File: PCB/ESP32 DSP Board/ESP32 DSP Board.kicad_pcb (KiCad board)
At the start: 2 copper layers, 67 parts, among them J1 USB4216-03-A_REVA, J2 USB4216-03-A_REVA, SW1 PTS810_SJM_250_SMTR_LFS, SW2 PTS810_SJM_250_SMTR_LFS, U11 INTERFACE-CP2102-GMR_QFN28_, U8 ESP32-S3-WROOM-1, U9 TPS73733DCQ

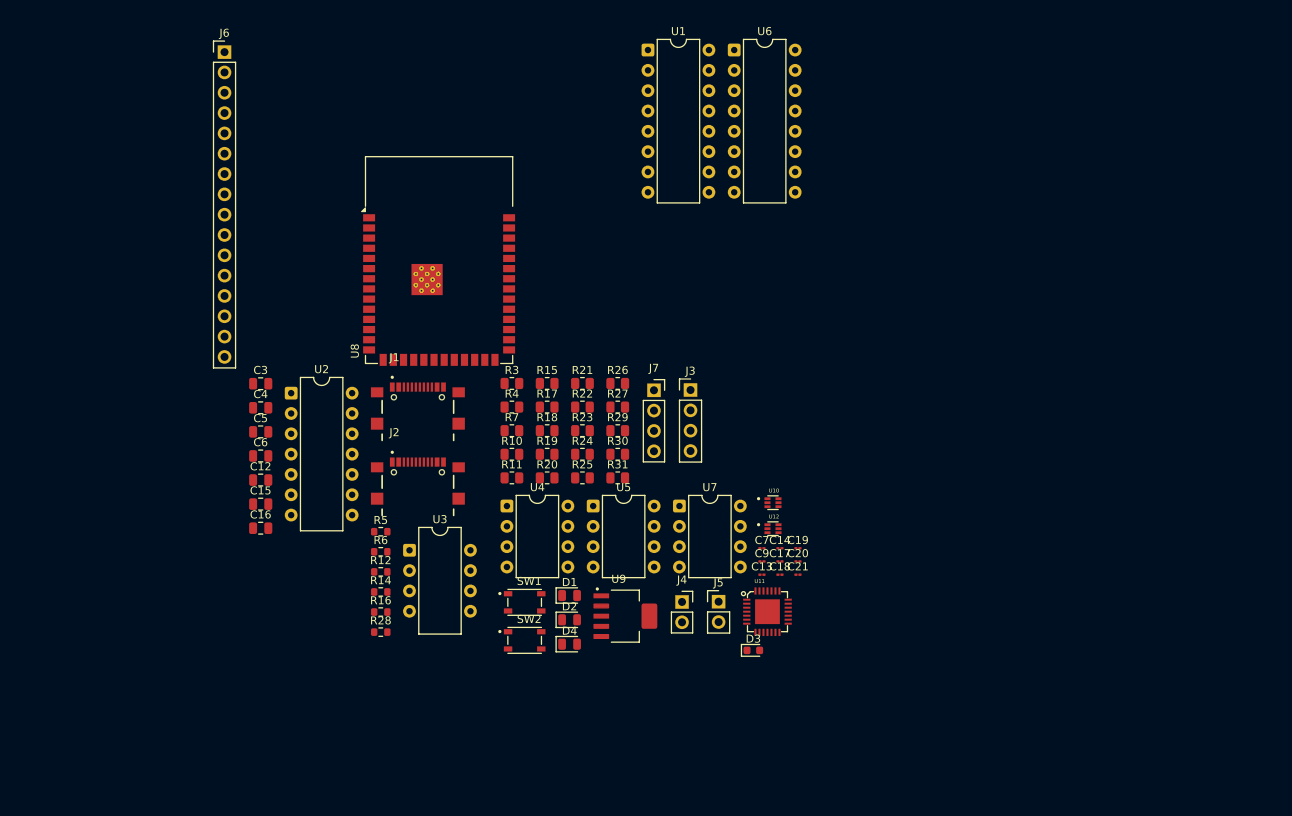
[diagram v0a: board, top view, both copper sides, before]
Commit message: Added clamping and biasing to audio inputs, hpf and rail to rail amplifier to DAC output, 1.5V LDO, footprints updated
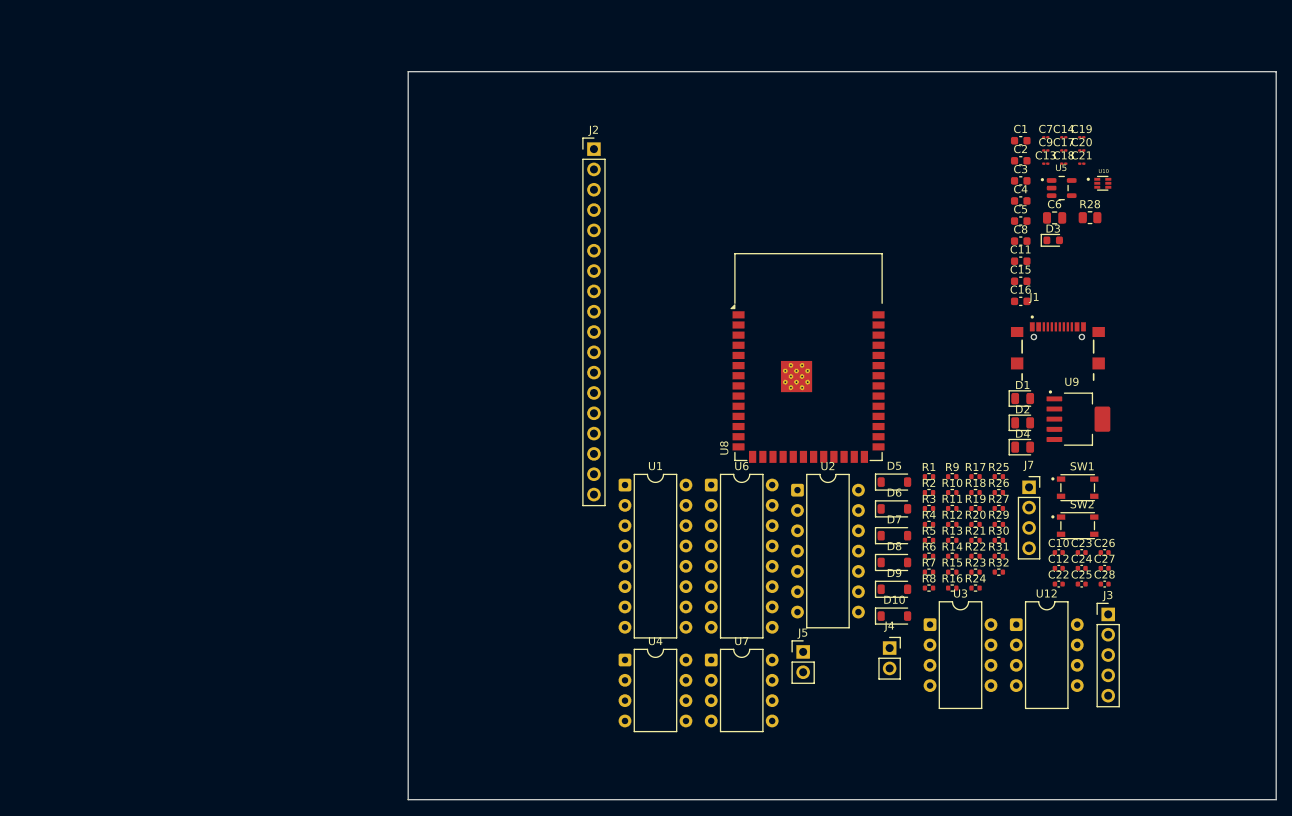
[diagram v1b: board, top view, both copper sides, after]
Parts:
- removed J6: ~, Connector_PinHeader_2.54mm:PinHeader_1x16_P2.54mm_Vertical
- removed U11: INTERFACE-CP2102-GMR_QFN28_, USB-UART-Bridge:CP2102-QFN28G
- added C1: 10uF, Capacitor_SMD:C_0603_1608Metric, F.Cu at (171.1, 55.6)
- added C10: 0.1uF, Capacitor_SMD:C_0402_1005Metric, F.Cu at (175.8, 107.1)
- added C11: 10uF, Capacitor_SMD:C_0603_1608Metric, F.Cu at (171.1, 70.7)
- added C2: 10uF, Capacitor_SMD:C_0603_1608Metric, F.Cu at (171.1, 58.1)
- added C22: 0.1uF, Capacitor_SMD:C_0402_1005Metric, F.Cu at (175.8, 111.0)
- added C23: 0.1uF, Capacitor_SMD:C_0402_1005Metric, F.Cu at (178.7, 107.1)
- added C24: 0.1uF, Capacitor_SMD:C_0402_1005Metric, F.Cu at (178.7, 109.1)
- added C25: 0.1uF, Capacitor_SMD:C_0402_1005Metric, F.Cu at (178.7, 111.0)
- added C26: 0.1uF, Capacitor_SMD:C_0402_1005Metric, F.Cu at (181.6, 107.1)
- added C27: 0.1uF, Capacitor_SMD:C_0402_1005Metric, F.Cu at (181.6, 109.1)
- added C28: 10nF, Capacitor_SMD:C_0402_1005Metric, F.Cu at (181.6, 111.0)
- added C8: 1uF, Capacitor_SMD:C_0603_1608Metric, F.Cu at (171.1, 68.2)
- added D10: D_Zener, Diode_SMD:D_SOD-123, F.Cu at (155.3, 115.0)
- added D5: D_Zener, Diode_SMD:D_SOD-123, F.Cu at (155.3, 98.3)
- added D6: D_Zener, Diode_SMD:D_SOD-123, F.Cu at (155.3, 101.7)
- added D7: D_Zener, Diode_SMD:D_SOD-123, F.Cu at (155.3, 105.0)
- added D8: D_Zener, Diode_SMD:D_SOD-123, F.Cu at (155.3, 108.3)
- added D9: D_Zener, Diode_SMD:D_SOD-123, F.Cu at (155.3, 111.7)
- added R1: 10K, Resistor_SMD:R_0402_1005Metric, F.Cu at (159.6, 97.6)
- added R13: 10K, Resistor_SMD:R_0402_1005Metric, F.Cu at (162.5, 105.6)
- added R2: 10K, Resistor_SMD:R_0402_1005Metric, F.Cu at (159.6, 99.6)
- added R32: 95.3K, Resistor_SMD:R_0402_1005Metric, F.Cu at (168.3, 109.6)
- added R8: 10K, Resistor_SMD:R_0402_1005Metric, F.Cu at (159.6, 111.5)
- added R9: 10K, Resistor_SMD:R_0402_1005Metric, F.Cu at (162.5, 97.6)
- C12: value 10uF -> 0.1uF; footprint Capacitor_SMD:C_0805_2012Metric -> Capacitor_SMD:C_0402_1005Metric
- C15, C16, C3, C4, C5: footprint Capacitor_SMD:C_0805_2012Metric -> Capacitor_SMD:C_0603_1608Metric
- J2: value USB4216-03-A_REVA -> ~; footprint USB_Connector:GCT_USB4216-03-A_REVA -> Connector_PinHeader_2.54mm:PinHeader_1x18_P2.54mm_Vertical
- J3: footprint Connector_PinHeader_2.54mm:PinHeader_1x04_P2.54mm_Vertical -> Connector_PinHeader_2.54mm:PinHeader_1x05_P2.54mm_Vertical
- R10, R11: value 5.1k -> 10K; footprint Resistor_SMD:R_0805_2012Metric -> Resistor_SMD:R_0402_1005Metric
- R12: value 1K -> 10K; footprint Resistor_SMD:R_0603_1608Metric -> Resistor_SMD:R_0402_1005Metric
- R14, R5, R6: footprint Resistor_SMD:R_0603_1608Metric -> Resistor_SMD:R_0402_1005Metric
- R15: value 470 -> 1K; footprint Resistor_SMD:R_0805_2012Metric -> Resistor_SMD:R_0402_1005Metric
- R16: value 220 -> 23.2K; footprint Resistor_SMD:R_0603_1608Metric -> Resistor_SMD:R_0402_1005Metric
- R17, R18, R19, R20, R21, R22, R23, R24, R25, R26, R27, R29, R3, R30, R31, R4, R7: footprint Resistor_SMD:R_0805_2012Metric -> Resistor_SMD:R_0402_1005Metric
- R28: footprint Resistor_SMD:R_0603_1608Metric -> Resistor_SMD:R_0805_2012Metric
- U12: footprint USB_ESD:USBLC6-2P6 -> Package_DIP:CERDIP-8_W7.62mm_SideBrazed
- U5: footprint Package_DIP:DIP-8_W7.62mm -> LDO_Adjustable:TPS73601DBVT
- moved C6 103.6 mm to (175.3, 65.3)
- moved R28 102.7 mm to (179.7, 65.2)
- moved C12 100.4 mm to (175.8, 109.1)
- moved C16 99.1 mm to (171.1, 75.7)
- moved C15 99.0 mm to (171.1, 73.2)
- moved C5 98.6 mm to (171.1, 65.7)
- moved C4 98.5 mm to (171.1, 63.2)
- moved C3 98.3 mm to (171.1, 60.6)
- moved J1 80.4 mm to (175.7, 82.3)
- moved R12 71.7 mm to (162.5, 103.6)
- moved R14 71.6 mm to (162.5, 107.6)
- moved R16 71.5 mm to (162.5, 111.5)
- moved U5 70.8 mm to (176.2, 61.5)
- moved SW1 70.6 mm to (178.2, 99.0)
- moved SW2 70.6 mm to (178.2, 103.8)
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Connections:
- C12 pad 1: +3V3 -> +5V
- C18 pad 2: Net-(U2-CH0) -> CH0_FOUT
- C20 pad 2: Net-(U2-CH1) -> CH1_FOUT
- J5 pad 1: DAC OUT -> Net-(C8-Pad1)
- R10 pad 1: GND -> CH1_FOUT
- R10 pad 2: Net-(J2-CC1) -> Net-(D8-A)
- R11 pad 1: Net-(J2-CC2) -> Net-(D8-A)
- R12 pad 2: +3.3V -> 1.5V
- R15 pad 1: Net-(U3-Zener_Cathode) -> Net-(C8-Pad1)
- R15 pad 2: Net-(R15-Pad2) -> GND
- R16 pad 1: Net-(R15-Pad2) -> 1.5V
- R16 pad 2: +5V -> Net-(U5-NR/FB)
- R19 pad 2: Net-(U5-Inv_Input) -> Net-(U12-In-)
- R20 pad 1: CH0 OUT -> Net-(U12-OUT)
- R21 pad 1: CH0 OUT -> Net-(U12-OUT)
- R22 pad 1: CH0 OUT -> Net-(U12-OUT)
- R23 pad 1: CH0 OUT -> Net-(U12-OUT)
- U10 pad 3: Net-(J1-DP1) -> USB D-
- U10 pad 6: USB D- -> Net-(J1-DP1)
- U12 pad 1: Net-(U11-D+) -> unconnected-(U12-NC-Pad1)
- U12 pad 2: GND -> Net-(U12-In-)
- U12 pad 3: Net-(J2-DP1) -> DAC OUT
- U12 pad 4: Net-(J2-DN1) -> GND
- U12 pad 5: +5V -> unconnected-(U12-NC-Pad5)
- U12 pad 6: Net-(U11-D-) -> Net-(U12-OUT)
- U2 pad 1: Net-(U2-CH0) -> CH0 IN
- U2 pad 2: Net-(U2-CH1) -> CH1 IN
- U3 pad 1: Net-(U3-Zener_Cathode) -> unconnected-(U3-Zener_Cathode-Pad1)
- U4 pad 1: Net-(U2-CH0) -> CH0_FOUT
- U4 pad 2: unconnected-(U4-1IN--Pad2) -> CH0_FOUT
- U4 pad 5: unconnected-(U4-2IN+-Pad5) -> CH1_FOUT
- U4 pad 7: Net-(U2-CH1) -> CH1_FOUT
- U5 pad 1: unconnected-(U5-Offset_Null-Pad1) -> +5V
- U5 pad 2: Net-(U5-Inv_Input) -> GND
- U5 pad 3: DAC OUT -> +5V
- U5 pad 4: GND -> Net-(U5-NR/FB)
- U5 pad 5: unconnected-(U5-Offset_Null-Pad5) -> 1.5V
- U6 pad 3: Net-(U5-Inv_Input) -> Net-(U12-In-)
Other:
- board outline added: 108.5 x 91 mm
- copper layers 2 -> 4

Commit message: PCB started, layers etup, analog layout started
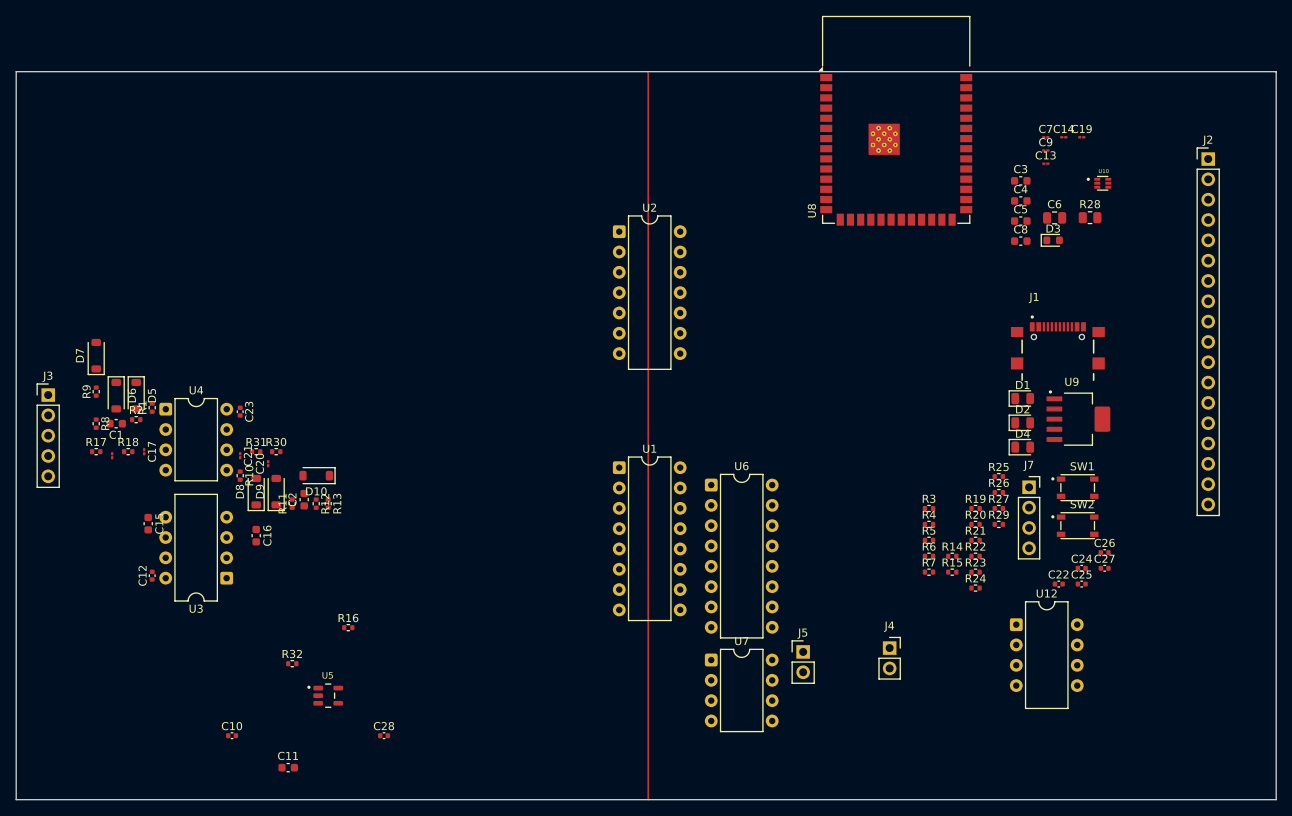
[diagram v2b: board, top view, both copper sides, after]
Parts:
- moved J3 135.3 mm to (49.5, 87.4)
- moved C18 124.4 mm to (57.5, 95.0), turned to -90 degrees
- moved C17 121.0 mm to (61.5, 94.5), turned to -90 degrees
- moved C1 118.5 mm to (58.0, 91.0), turned to 180 degrees
- moved C12 113.3 mm to (62.5, 110.0), turned to 90 degrees
- moved C15 113.2 mm to (62.0, 103.5), turned to -90 degrees
- moved U5 111.5 mm to (84.5, 125.0)
- moved C21 111.4 mm to (73.5, 95.0), turned to -90 degrees
- moved C11 111.3 mm to (79.5, 134.0)
- moved R17 110.0 mm to (55.5, 94.5)
- moved C20 109.0 mm to (77.0, 96.0), turned to 90 degrees
- moved R9 107.5 mm to (55.5, 87.0), turned to 90 degrees
- moved C23 106.7 mm to (73.5, 89.5), turned to -90 degrees
- moved R8 106.1 mm to (55.5, 91.0), turned to -90 degrees
- moved R18 106.0 mm to (59.5, 94.5)
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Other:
- board size 108.5 x 91 mm -> 157.5 x 91 mm

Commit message: pcb component layout finished, ic and pin header footprints fixed
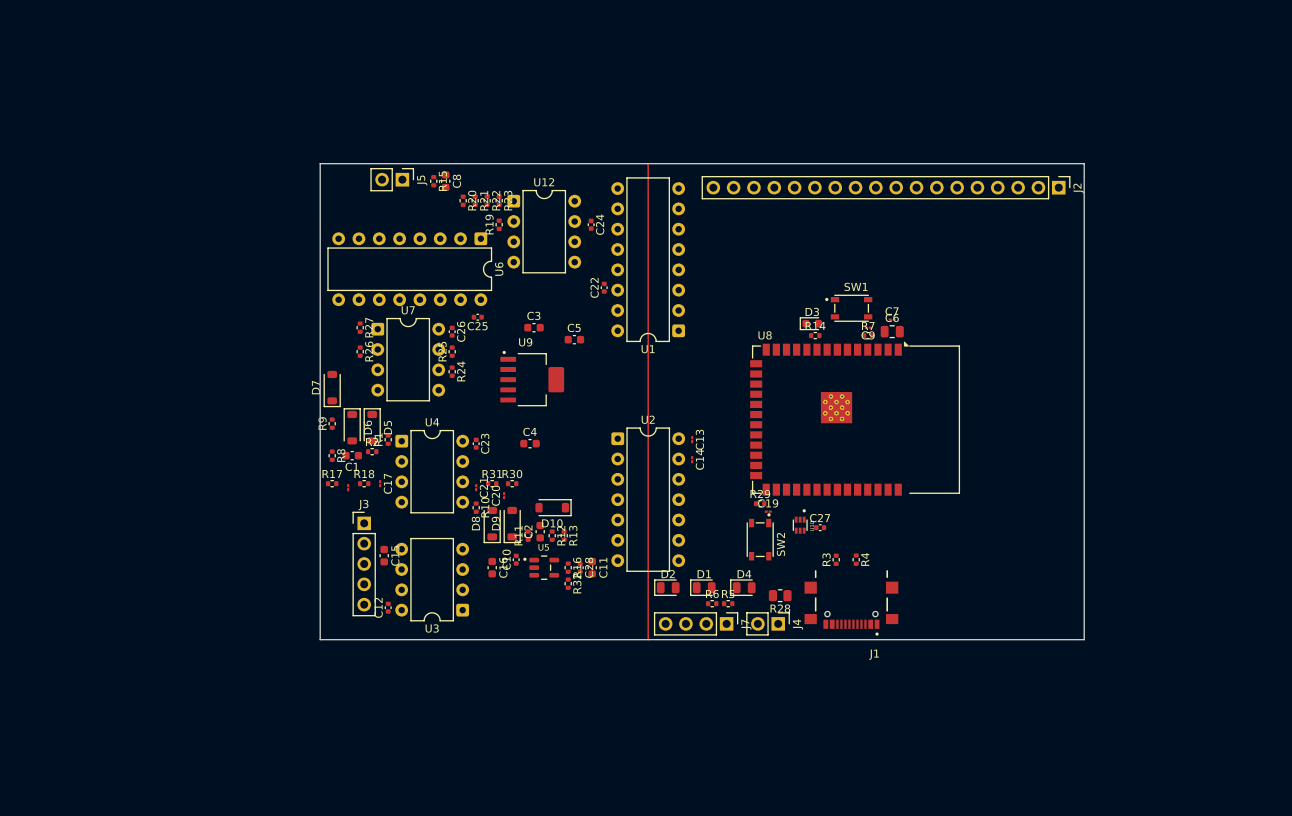
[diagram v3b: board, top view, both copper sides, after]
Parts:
- J4: footprint Connector_PinSocket_2.54mm:PinSocket_1x02_P2.54mm_Vertical -> Connector_PinHeader_2.54mm:PinHeader_1x02_P2.54mm_Vertical
- J7: footprint Connector_PinSocket_2.54mm:PinSocket_1x04_P2.54mm_Vertical -> Connector_PinHeader_2.54mm:PinHeader_1x04_P2.54mm_Vertical
- U1: footprint Package_DIP:CERDIP-16_W7.62mm_SideBrazed -> Package_DIP:DIP-16_W7.62mm
- U12, U3: footprint Package_DIP:CERDIP-8_W7.62mm_SideBrazed -> Package_DIP:DIP-8_W7.62mm
- U2: footprint Package_DIP:CERDIP-14_W7.62mm_SideBrazed -> Package_DIP:DIP-14_W7.62mm
- moved C26 86.1 mm to (100.0, 79.5), turned to -90 degrees
- moved R27 83.0 mm to (88.5, 79.0), turned to -90 degrees
- moved C25 82.5 mm to (103.2, 77.7), turned to 180 degrees
- moved U12 82.1 mm to (107.7, 63.2)
- moved R26 81.7 mm to (88.5, 82.0), turned to -90 degrees
- moved R15 81.2 mm to (97.7, 60.7), turned to -90 degrees
- moved J5 77.4 mm to (93.8, 60.5), turned to -90 degrees
- moved R20 75.8 mm to (101.4, 63.1), turned to -90 degrees
- moved R21 75.6 mm to (102.9, 63.1), turned to -90 degrees
- moved R22 75.5 mm to (104.4, 63.1), turned to -90 degrees
- moved R23 75.5 mm to (105.9, 63.1), turned to -90 degrees
- moved C24 74.9 mm to (117.4, 66.1), turned to -90 degrees
- moved C8 72.3 mm to (99.2, 60.7), turned to -90 degrees
- moved R24 70.8 mm to (100.0, 84.5), turned to -90 degrees
- moved R25 70.1 mm to (100.0, 82.0), turned to 90 degrees
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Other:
- board size 157.5 x 91 mm -> 95.5 x 59.5 mm

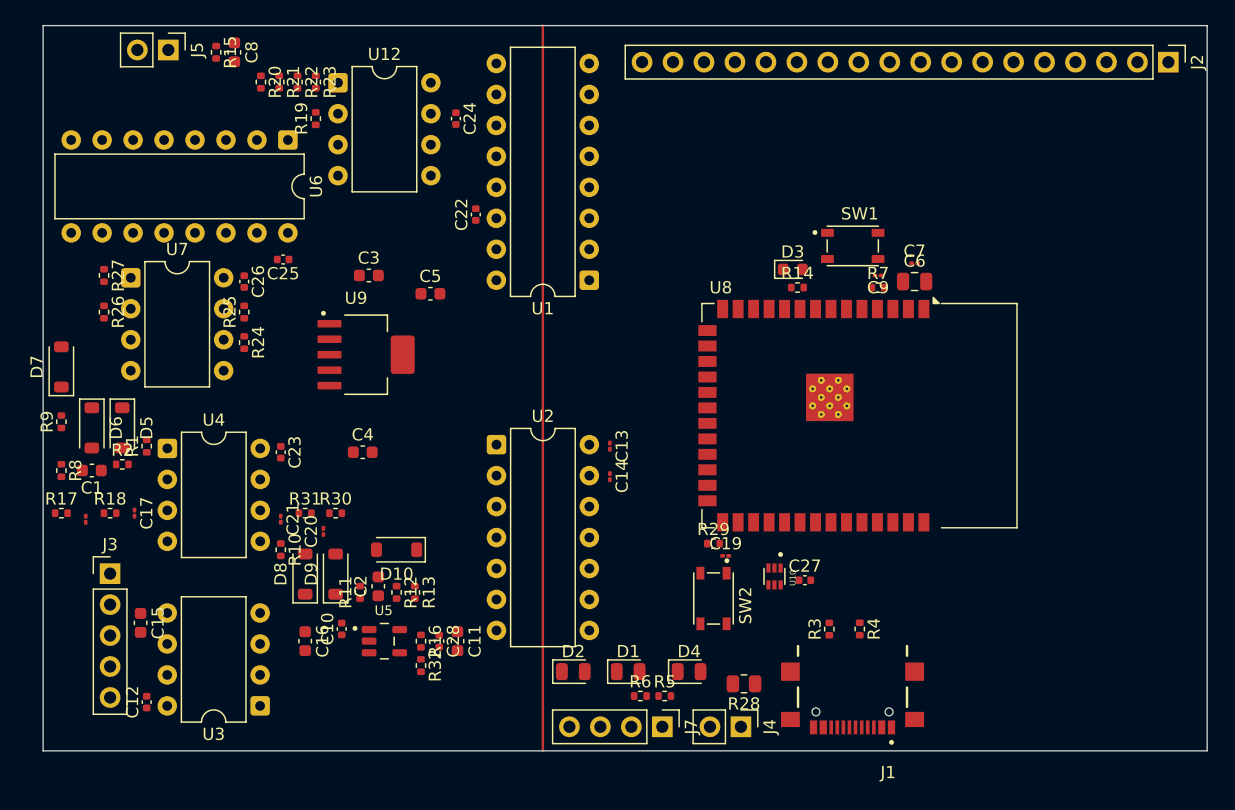
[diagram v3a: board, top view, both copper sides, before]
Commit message: U3 and U4 routing completed, 5V and GND plane added
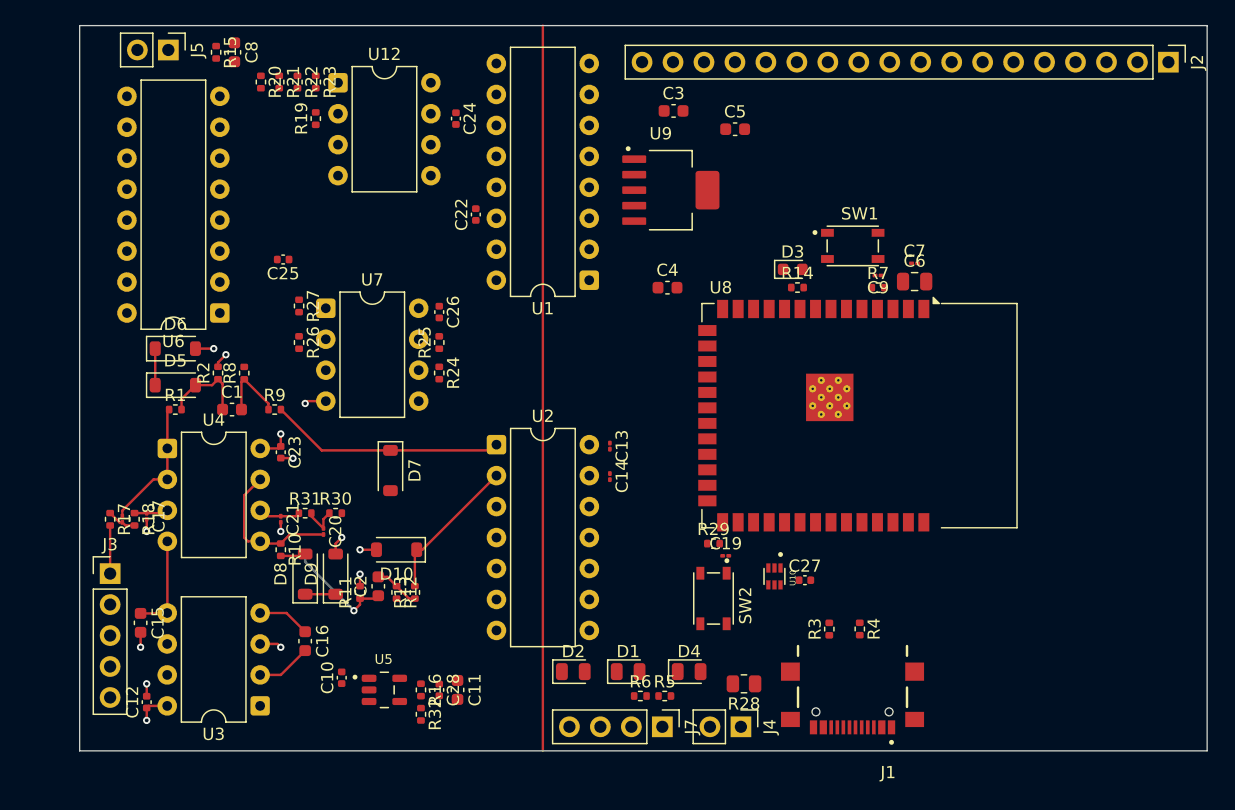
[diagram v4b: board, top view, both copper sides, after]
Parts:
- moved C3 28.4 mm to (135.2, 65.5)
- moved C4 28.4 mm to (134.7, 80.0)
- moved C5 28.4 mm to (140.3, 67.0)
- moved U9 28.4 mm to (135.0, 72.0)
- moved D7 28.3 mm to (112.0, 95.0), turned to -90 degrees
- moved R9 17.5 mm to (102.5, 90.0), turned to 0 degrees
- moved R8 17.0 mm to (100.0, 87.0), turned to 90 degrees
- moved C26 16.2 mm to (116.0, 82.0)
- moved R24 16.2 mm to (116.0, 87.0)
- moved R25 16.2 mm to (116.0, 84.5)
- moved R26 16.2 mm to (104.5, 84.5)
- moved R27 16.2 mm to (104.5, 81.5)
- moved U7 16.2 mm to (106.7, 81.7)
- moved U6 15.3 mm to (98.0, 82.1), turned to 180 degrees
- moved C1 12.5 mm to (99.0, 90.0), turned to 0 degrees
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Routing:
- net CH0 IN: track 0.00 -> 19.3 mm
- net GND: track 0.00 -> 15.2 mm, vias 0 -> 12
- net CH1_FOUT: track 0.00 -> 12.3 mm
- net CH1 IN: track 0.00 -> 12.1 mm
- net CH0_FOUT: track 0.00 -> 11.5 mm
- net Net-(D8-A): track 0.00 -> 11.0 mm, vias 0 -> 1
- net -5V: track 0.00 -> 8.08 mm
- net Net-(D5-A): track 0.00 -> 7.17 mm
- net Net-(C1-Pad2): track 0.00 -> 5.90 mm
- net +5V: track 0.00 -> 5.55 mm, vias 0 -> 2
- net Net-(U3-C+): track 0.00 -> 4.52 mm
- net Net-(U3-C-): track 0.00 -> 4.33 mm
- net ADC CH0: track 0.00 -> 3.95 mm
- net Net-(C2-Pad2): track 0.00 -> 3.74 mm
- net Net-(U4-2IN-): track 0.00 -> 3.48 mm
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- added copper zone on In2.Cu, net +5V
- added copper zone on In1.Cu, net GND
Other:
- board size 95.5 x 59.5 mm -> 92.5 x 59.5 mm
